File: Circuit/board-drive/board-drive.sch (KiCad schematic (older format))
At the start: 13 parts

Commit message: edited lib and driver board sch
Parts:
- removed P?: XT30, symbol XT30
- removed U?: Polulu_Maestro12, symbol Polulu_Maestro12
- removed U? (x9): Polulu_SimpleMotorController24v23, symbol Polulu_SimpleMotorController24v23
- added P? (x8): XT30, symbol XT30
- added U?: Pololu_Maestro12, symbol Pololu_Maestro12
- added U? (x8): Pololu_SimpleMotorController24v23, symbol Pololu_SimpleMotorController24v23
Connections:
- net labels added: +5V, GNDD, OUTA_0, OUTA_1, OUTA_2, OUTA_3, OUTA_4, OUTA_5, OUTA_6, OUTA_7, OUTB_0, OUTB_1, OUTB_2, OUTB_3, OUTB_4, OUTB_5, OUTB_6, OUTB_7
- net labels removed: GND, VCC, outA, outB
- wire segments 52 -> 68

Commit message: edited sch
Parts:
- added P10, P9: XT60, symbol XT60
- P1, P2, P3, P4, P5, P6, P7, P8: renamed from P?; footprint (none) -> zeabus:XT30
- U1: renamed from U?; footprint (none) -> zeabus:Pololu_Maestro12
- U10, U11, U4, U5, U6, U7, U8, U9: renamed from U?; footprint (none) -> zeabus:pololu_motorcontroller24v23
- U2, U3: renamed from U?; footprint (none) -> zeabus:Narrow-SOIC-16
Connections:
- removed net +BATT: U10.~ (Vin), U11.~ (Vin), U4.~ (Vin), U5.~ (Vin), U6.~ (Vin), U7.~ (Vin), U8.~ (Vin), U9.~ (Vin)
- removed net GNDPWR: U10.~ (Vin), U11.~ (Vin), U4.~ (Vin), U5.~ (Vin), U6.~ (Vin), U7.~ (Vin), U8.~ (Vin), U9.~ (Vin)
- new net BATTGND_0: P9.2 (P2), U4.~ (Vin), U5.~ (Vin), U6.~ (Vin), U7.~ (Vin)
- new net BATTGND_1: P10.2 (P2), U10.~ (Vin), U11.~ (Vin), U8.~ (Vin), U9.~ (Vin)
- new net BATTIN_0: P9.1 (P1), U4.~ (Vin), U5.~ (Vin), U6.~ (Vin), U7.~ (Vin)
- new net BATTIN_1: P10.1 (P1), U10.~ (Vin), U11.~ (Vin), U8.~ (Vin), U9.~ (Vin)
- no-connect marks 0 -> 14

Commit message: PCB routed prototype1
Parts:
- removed U10, U11, U4, U5, U6, U7, U8, U9: Pololu_SimpleMotorController24v23, zeabus:pololu_motorcontroller24v23, symbol Pololu_SimpleMotorController24v23
- added U10, U11, U16, U17, U18, U19, U8, U9: PowerDist_WiretoBoard, zeabus:PowerDist_WiretoBoard, symbol PowerDist_WiretoBoard
- added U12, U13, U14, U15, U4, U5, U6, U7: Pololu_SimpleMotorController24v23_withnoPowerDist, zeabus:pololu_motorcontroller24v23, symbol Pololu_SimpleMotorController24v23_withnoPowerDist
- P10, P9: footprint (none) -> zeabus:XT60
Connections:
- net labels added: BATTGND
- net labels removed: BATTGND_0, BATTGND_1, signl6
- wire segments 88 -> 89
- no-connect marks 14 -> 13
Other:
- moved on the sheet: P1, P2, P3, P4, P5, P6, P7, P8, U2, U3

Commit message: edited sch and pcb
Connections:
- net labels added: +5v_BEC
- wire segments 89 -> 87
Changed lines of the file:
@@
 NoConn ~ 8250 5500
 NoConn ~ 8250 4000
-NoConn ~ 8250 2500
 NoConn ~ 8250 1000
 NoConn ~ 5350 5100
@@
 Wire Wire Line
 	6800 6200 6350 6200
-Wire Wire Line
-	4250 2500 5250 2500
-Wire Wire Line
-	4850 2500 4850 5100
-Wire Wire Line
-	4850 5100 4250 5100
-Connection ~ 4850 2500
+Text Label 4250 2500 0    60   ~ 0
++5v_BEC
+Text Label 4250 5100 0    60   ~ 0
++5v_BEC
+Text Label 7900 2500 0    60   ~ 0
++5v_BEC
+Wire Wire Line
+	7900 2500 8250 2500
+NoConn ~ 5250 2500
 $EndSCHEMATC

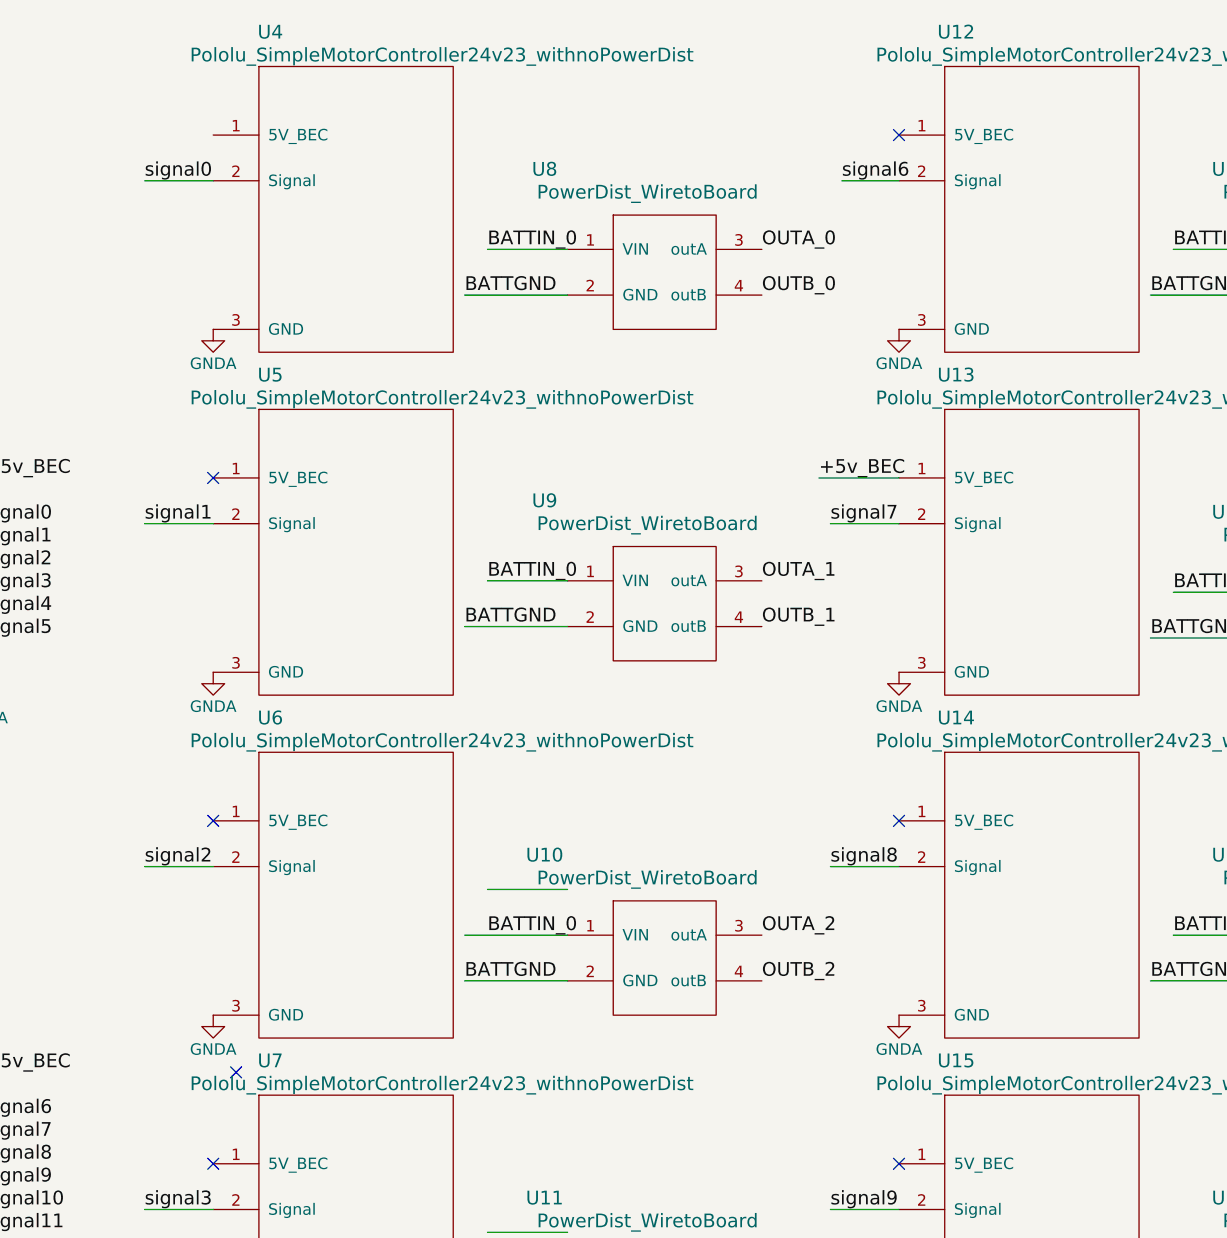
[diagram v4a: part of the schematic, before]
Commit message: edit PCB layout and label component
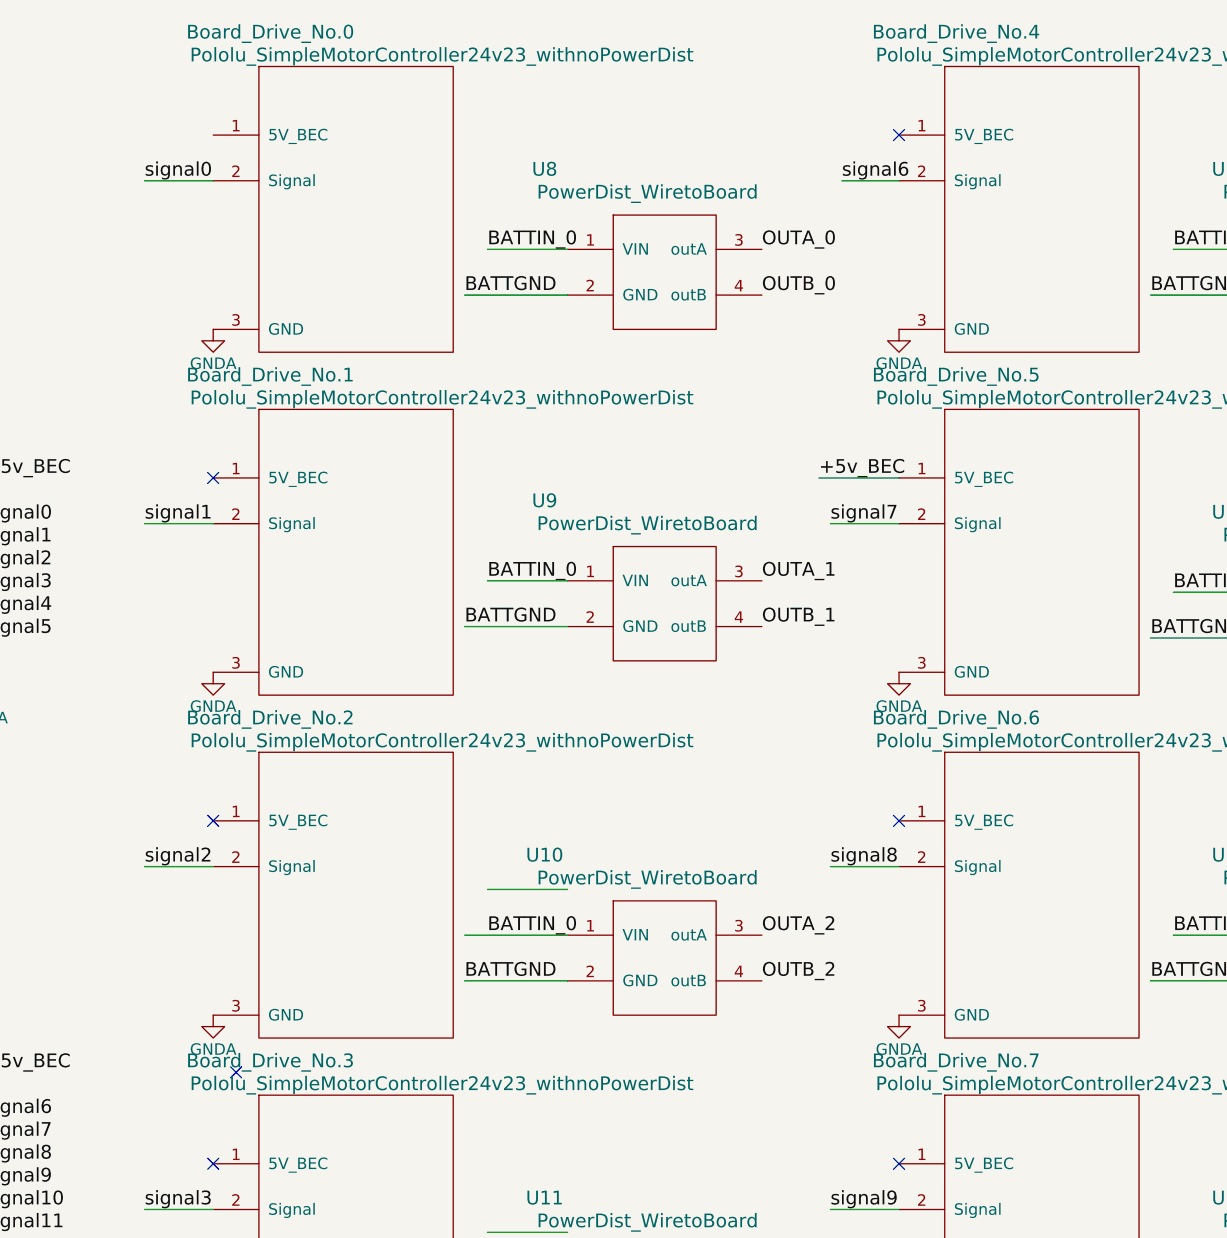
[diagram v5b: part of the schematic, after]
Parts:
- renumbered U4 to Board_Drive_No.0, U5 to Board_Drive_No.1, U6 to Board_Drive_No.2, U7 to Board_Drive_No.3, U12 to Board_Drive_No.4, U13 to Board_Drive_No.5, U14 to Board_Drive_No.6, U15 to Board_Drive_No.7
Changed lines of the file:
@@
 LIBS:contrib
 LIBS:valves
-LIBS:zeabus
 LIBS:board-drive-cache
 EELAYER 25 0
@@
 $EndComp
 $Comp
-L Pololu_SimpleMotorController24v23_withnoPowerDist U7
+L Pololu_SimpleMotorController24v23_withnoPowerDist Board_Drive_No.3
 U 1 1 5A5AF0D1
 P 5900 5950
-F 0 "U7" H 5500 6850 60  0000 C CNN
+F 0 "Board_Drive_No.3" H 5500 6850 60  0000 C CNN
 F 1 "Pololu_SimpleMotorController24v23_withnoPowerDist" H 6250 6750 60  0000 C CNN
 F 2 "zeabus:pololu_motorcontroller24v23" H 6250 6750 60  0001 C CNN
@@
 $EndComp
 $Comp
-L Pololu_SimpleMotorController24v23_withnoPowerDist U6
+L Pololu_SimpleMotorController24v23_withnoPowerDist Board_Drive_No.2
 U 1 1 5A5AF030
 P 5900 4450
-F 0 "U6" H 5500 5350 60  0000 C CNN
+F 0 "Board_Drive_No.2" H 5500 5350 60  0000 C CNN
 F 1 "Pololu_SimpleMotorController24v23_withnoPowerDist" H 6250 5250 60  0000 C CNN
 F 2 "zeabus:pololu_motorcontroller24v23" H 6250 5250 60  0001 C CNN
@@
 $EndComp
 $Comp
-L Pololu_SimpleMotorController24v23_withnoPowerDist U5
+L Pololu_SimpleMotorController24v23_withnoPowerDist Board_Drive_No.1
 U 1 1 5A5AEF8D
 P 5900 2950
-F 0 "U5" H 5500 3850 60  0000 C CNN
+F 0 "Board_Drive_No.1" H 5500 3850 60  0000 C CNN
 F 1 "Pololu_SimpleMotorController24v23_withnoPowerDist" H 6250 3750 60  0000 C CNN
 F 2 "zeabus:pololu_motorcontroller24v23" H 6250 3750 60  0001 C CNN
@@
 $EndComp
 $Comp
-L Pololu_SimpleMotorController24v23_withnoPowerDist U4
+L Pololu_SimpleMotorController24v23_withnoPowerDist Board_Drive_No.0
 U 1 1 5A5AE339
 P 5900 1450
-F 0 "U4" H 5500 2350 60  0000 C CNN
+F 0 "Board_Drive_No.0" H 5500 2350 60  0000 C CNN
 F 1 "Pololu_SimpleMotorController24v23_withnoPowerDist" H 6250 2250 60  0000 C CNN
 F 2 "zeabus:pololu_motorcontroller24v23" H 6250 2250 60  0001 C CNN
@@
 $EndComp
 $Comp
-L Pololu_SimpleMotorController24v23_withnoPowerDist U15
+L Pololu_SimpleMotorController24v23_withnoPowerDist Board_Drive_No.7
 U 1 1 5A5AFE93
 P 8900 5950
-F 0 "U15" H 8500 6850 60  0000 C CNN
+F 0 "Board_Drive_No.7" H 8500 6850 60  0000 C CNN
 F 1 "Pololu_SimpleMotorController24v23_withnoPowerDist" H 9250 6750 60  0000 C CNN
 F 2 "zeabus:pololu_motorcontroller24v23" H 9250 6750 60  0001 C CNN
@@
 $EndComp
 $Comp
-L Pololu_SimpleMotorController24v23_withnoPowerDist U14
+L Pololu_SimpleMotorController24v23_withnoPowerDist Board_Drive_No.6
 U 1 1 5A5AFE9F
 P 8900 4450
-F 0 "U14" H 8500 5350 60  0000 C CNN
+F 0 "Board_Drive_No.6" H 8500 5350 60  0000 C CNN
 F 1 "Pololu_SimpleMotorController24v23_withnoPowerDist" H 9250 5250 60  0000 C CNN
 F 2 "zeabus:pololu_motorcontroller24v23" H 9250 5250 60  0001 C CNN
@@
 $EndComp
 $Comp
-L Pololu_SimpleMotorController24v23_withnoPowerDist U13
+L Pololu_SimpleMotorController24v23_withnoPowerDist Board_Drive_No.5
 U 1 1 5A5AFEAB
 P 8900 2950
-F 0 "U13" H 8500 3850 60  0000 C CNN
+F 0 "Board_Drive_No.5" H 8500 3850 60  0000 C CNN
 F 1 "Pololu_SimpleMotorController24v23_withnoPowerDist" H 9250 3750 60  0000 C CNN
 F 2 "zeabus:pololu_motorcontroller24v23" H 9250 3750 60  0001 C CNN
@@
 $EndComp
 $Comp
-L Pololu_SimpleMotorController24v23_withnoPowerDist U12
+L Pololu_SimpleMotorController24v23_withnoPowerDist Board_Drive_No.4
 U 1 1 5A5AFEB7
 P 8900 1450
-F 0 "U12" H 8500 2350 60  0000 C CNN
+F 0 "Board_Drive_No.4" H 8500 2350 60  0000 C CNN
 F 1 "Pololu_SimpleMotorController24v23_withnoPowerDist" H 9250 2250 60  0000 C CNN
 F 2 "zeabus:pololu_motorcontroller24v23" H 9250 2250 60  0001 C CNN

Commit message: edited pcb
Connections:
- wire segments 87 -> 85
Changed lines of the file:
@@
 LIBS:contrib
 LIBS:valves
+LIBS:zeabus
 LIBS:board-drive-cache
 EELAYER 25 0
@@
 	6800 3150 6350 3150
 Wire Wire Line
-	6450 4300 6800 4300
-Wire Wire Line
-	6800 4500 6350 4500
-Wire Wire Line
-	6450 5800 6800 5800
-Wire Wire Line
-	6800 6000 6350 6000
-Wire Wire Line
 	9350 6200 9800 6200
 Wire Wire Line
@@
 	7900 2500 8250 2500
 NoConn ~ 5250 2500
+Wire Wire Line
+	6450 4500 6800 4500
+Wire Wire Line
+	6450 6000 6800 6000
 $EndSCHEMATC
